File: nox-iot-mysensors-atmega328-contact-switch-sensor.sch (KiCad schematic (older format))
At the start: 13 parts, among them J2 Magnet Switch, J3 FTDI, SW1 SW_Push, U1 ATmega328-PU, U3 NRF24L01, Y1 16Mhz

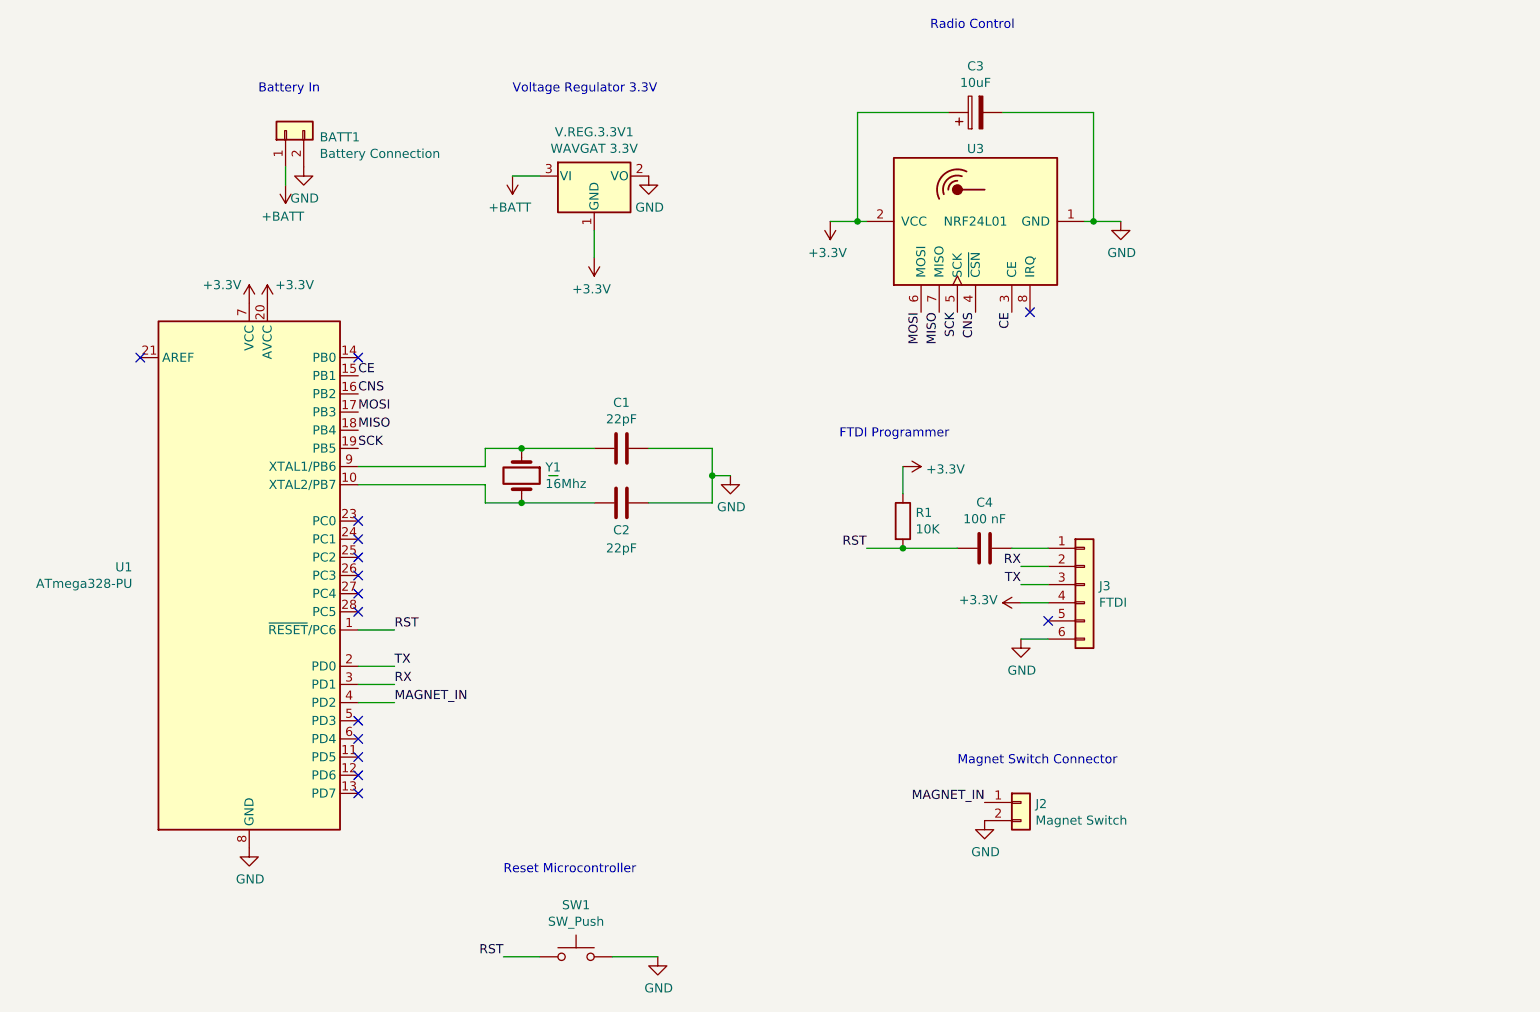
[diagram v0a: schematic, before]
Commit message: voltage divider for battery sensor
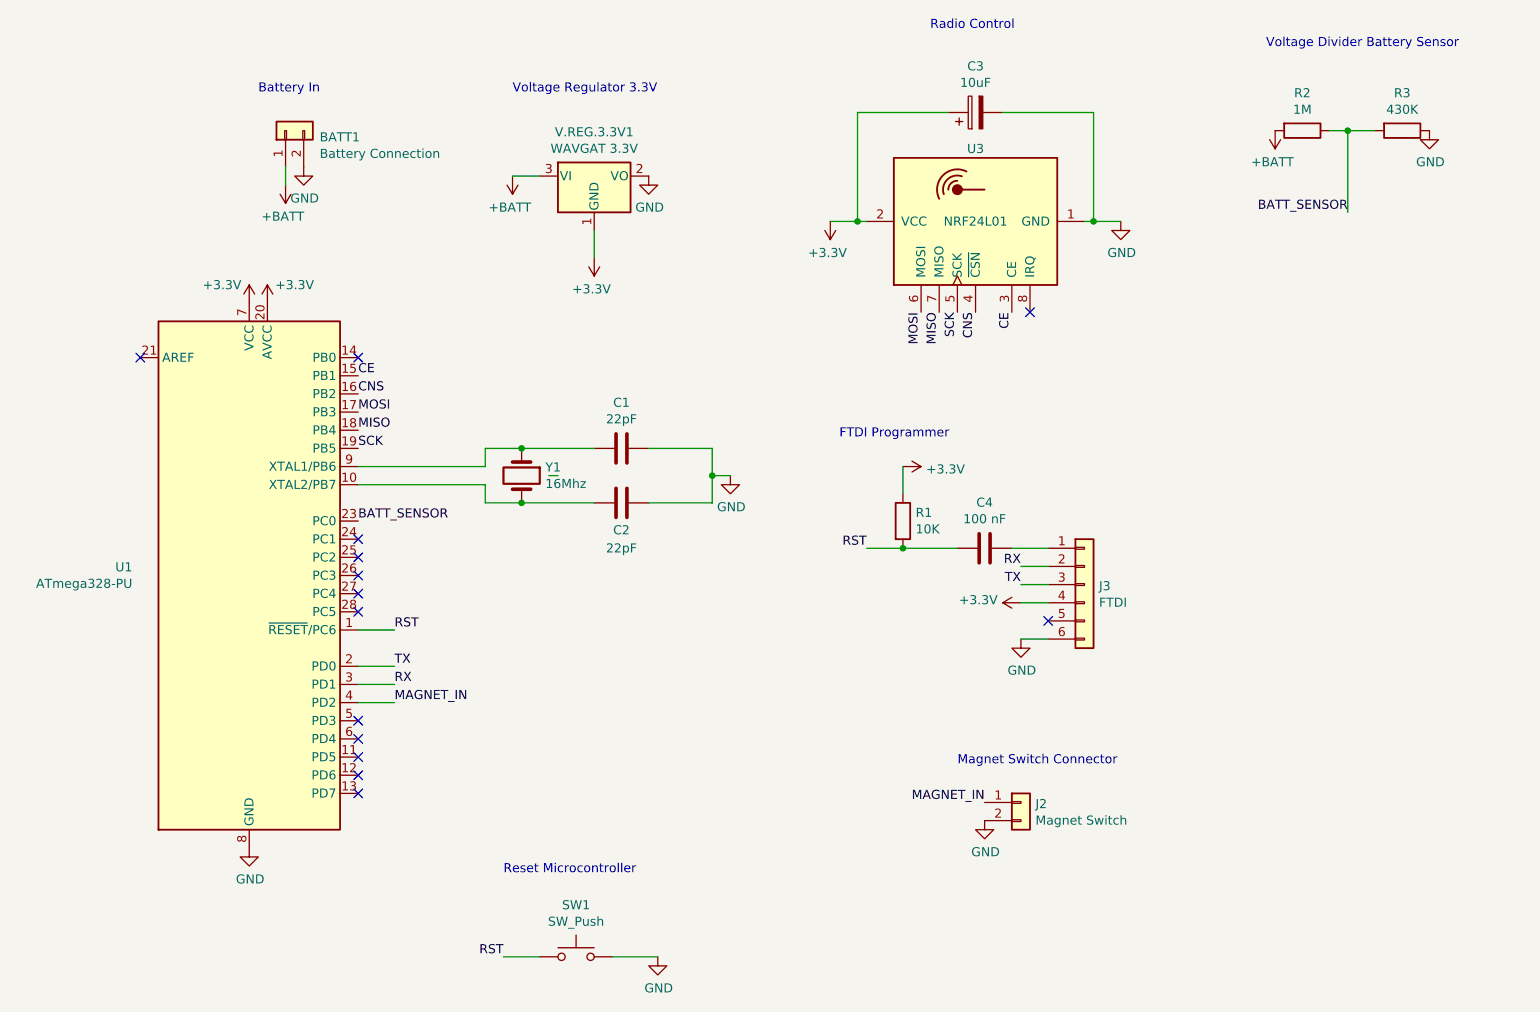
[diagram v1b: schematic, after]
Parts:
- added R2: 1M, Resistor_THT:R_Axial_DIN0207_L6.3mm_D2.5mm_P2.54mm_Vertical, symbol Device:R
- added R3: 430K, Resistor_THT:R_Axial_DIN0207_L6.3mm_D2.5mm_P2.54mm_Vertical, symbol Device:R
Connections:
- net labels added: BATT_SENSOR
- wire segments 39 -> 42
- no-connect marks 15 -> 14
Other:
- note added: "Voltage Divider Battery Sensor"
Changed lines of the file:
@@
 	1    0    0    -1
 $EndComp
-NoConn ~ 3650 3350
 NoConn ~ 3650 3450
 NoConn ~ 3650 3550
@@
 Wire Wire Line
 	6650 3050 6650 3200
+Text Notes 8650 750  0    50   ~ 0
+Voltage Divider Battery Sensor
+$Comp
+L Device:R R2
+U 1 1 6084408F
+P 8850 1200
+F 0 "R2" V 8643 1200 50  0000 C CNN
+F 1 "1M" V 8734 1200 50  0000 C CNN
+F 2 "Resistor_THT:R_Axial_DIN0207_L6.3mm_D2.5mm_P2.54mm_Vertical" V 8780 1200 50  0001 C CNN
+F 3 "~" H 8850 1200 50  0001 C CNN
+	1    8850 1200
+	0    1    1    0
+$EndComp
+$Comp
+L Device:R R3
+U 1 1 608448EF
+P 9400 1200
+F 0 "R3" V 9193 1200 50  0000 C CNN
+F 1 "430K" V 9284 1200 50  0000 C CNN
+F 2 "Resistor_THT:R_Axial_DIN0207_L6.3mm_D2.5mm_P2.54mm_Vertical" V 9330 1200 50  0001 C CNN
+F 3 "~" H 9400 1200 50  0001 C CNN
+	1    9400 1200
+	0    1    1    0
+$EndComp
+$Comp
+L power:GND #PWR0117
+U 1 1 60844EED
+P 9550 1200
+F 0 "#PWR0117" H 9550 950 50  0001 C CNN
+F 1 "GND" H 9555 1027 50  0000 C CNN
+F 2 "" H 9550 1200 50  0001 C CNN
+F 3 "" H 9550 1200 50  0001 C CNN
+	1    9550 1200
+	1    0    0    -1
+$EndComp
+Wire Wire Line
+	9000 1200 9100 1200
+$Comp
+L power:+BATT #PWR0118
+U 1 1 60846697
+P 8700 1200
+F 0 "#PWR0118" H 8700 1050 50  0001 C CNN
+F 1 "+BATT" H 8715 1373 50  0000 C CNN
+F 2 "" H 8700 1200 50  0001 C CNN
+F 3 "" H 8700 1200 50  0001 C CNN
+	1    8700 1200
+	-1   0    0    1
+$EndComp
+Text Label 9100 1650 2    50   ~ 0
+BATT_SENSOR
+Wire Wire Line
+	9100 1650 9100 1200
+Connection ~ 9100 1200
+Wire Wire Line
+	9100 1200 9250 1200
+Text Label 3650 3350 0    50   ~ 0
+BATT_SENSOR
 $EndSCHEMATC

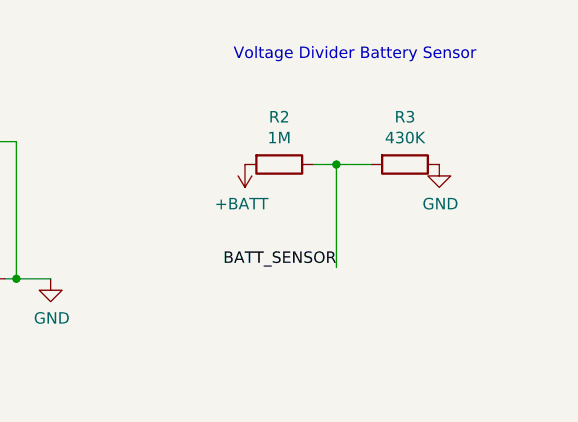
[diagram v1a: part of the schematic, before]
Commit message: updated with voltage divider value
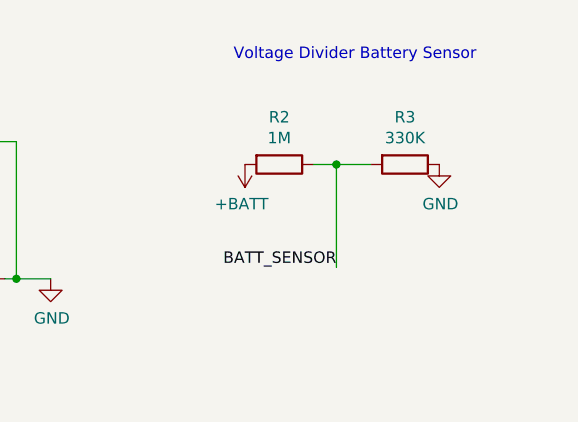
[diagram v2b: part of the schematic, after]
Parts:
- R3: value 430K -> 330K
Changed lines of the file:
@@
 P 9400 1200
 F 0 "R3" V 9193 1200 50  0000 C CNN
-F 1 "430K" V 9284 1200 50  0000 C CNN
+F 1 "330K" V 9284 1200 50  0000 C CNN
 F 2 "Resistor_THT:R_Axial_DIN0207_L6.3mm_D2.5mm_P2.54mm_Vertical" V 9330 1200 50  0001 C CNN
 F 3 "~" H 9400 1200 50  0001 C CNN
